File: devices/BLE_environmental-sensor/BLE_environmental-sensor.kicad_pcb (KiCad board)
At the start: 2 copper layers, 55 x 28 mm, 14 parts, among them Q1 Q_PMOS_GSD, U1 BGM220SC12WGA2R, U2 SHT4x, U3 STCC4, U4 LPS22DF, Y1 32.768kHz

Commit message: Finsihes version A.0 of the BLE sensor
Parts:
- removed Q1: Q_PMOS_GSD, Package_TO_SOT_SMD:TSOT-23
- removed Y1: 32.768kHz, Crystal:Crystal_SMD_3215-2Pin_3.2x1.5mm
- added C6: 100u, Capacitor_SMD:C_1206_3216Metric, F.Cu at (119.5, 94.0)
- added C7: 100n, Capacitor_SMD:C_0603_1608Metric, F.Cu at (123.8, 89.9)
- added J1: Samtec FTSM, Connector:Tag-Connect_TC2050-IDC-NL_2x05_P1.27mm_Vertical, F.Cu at (113.0, 79.2)
- added R2: 10k, Resistor_SMD:R_0603_1608Metric, F.Cu at (105.5, 75.3)
- added R3: 1M, Resistor_SMD:R_0603_1608Metric, F.Cu at (130.9, 93.2)
- added R4: 10k, Resistor_SMD:R_0603_1608Metric, F.Cu at (116.4, 89.8)
- added REF**: OSHW-Logo_19x20mm_SilkScreen, Symbol:OSHW-Logo_19x20mm_SilkScreen, B.Cu at (143.0, 84.0)
- added TP1: RCUCTE, custom:RCUCTE, F.Cu at (107.7, 95.9)
- added TP2: RCUCTE, custom:RCUCTE, F.Cu at (102.4, 94.1)
- added TP3: RCUCTE, custom:RCUCTE, F.Cu at (107.7, 93.9)
- added TP4: RCUCTE, custom:RCUCTE, F.Cu at (105.7, 72.7)
- added TP5: RCUCTE, custom:RCUCTE, F.Cu at (108.5, 72.7)
- added TP6: RCUCTE, custom:RCUCTE, F.Cu at (109.2, 83.8)
- added U5: TPS61291DVR, Package_SON:WSON-6-1EP_2x2mm_P0.65mm_EP1x1.6mm_ThermalVias, F.Cu at (115.0, 93.1)
- added U6: MX25R8035FM1IL0, Package_SO:JEITA_SOIC-8_3.9x4.9mm_P1.27mm, F.Cu at (128.3, 88.8)
- added kibuzzard-6A3D4B32: G***, kibuzzard-6A3D4B32, F.Cu at (110.8, 72.7)
- added kibuzzard-6A3D4B40: G***, kibuzzard-6A3D4B40, F.Cu at (103.3, 72.7)
- added kibuzzard-6A3D4B4B: G***, kibuzzard-6A3D4B4B, F.Cu at (102.4, 92.4)
- added kibuzzard-6A3D4B61: G***, kibuzzard-6A3D4B61, F.Cu at (105.4, 93.9)
- added kibuzzard-6A3D4B8C: G***, kibuzzard-6A3D4B8C, F.Cu at (105.3, 95.9)
- added kibuzzard-6A3D4E4D: G***, kibuzzard-6A3D4E4D, B.Cu at (113.0, 84.0)
- BT1: footprint custom:BatteryHolder_MPD_BK-912 -> custom:BatteryHolder_TE_BAT-HLD-001
- R1: value 0 -> 10k; footprint Resistor_SMD:R_01005_0402Metric -> Resistor_SMD:R_0603_1608Metric
- U1: value BGM220SC12WGA2R -> BGM220PC22HNA2; footprint custom:SiliconLab_BGM220SC12WGA2R -> custom:SiliconLab_BGM220P
- moved C1 61.0 mm to (117.3, 94.0), turned to 90 degrees
- moved C2 56.4 mm to (112.7, 94.0), turned to 90 degrees
- moved C3 51.0 mm to (104.6, 89.7)
- moved C4 50.4 mm to (104.6, 80.9), turned to 0 degrees
- moved L1 50.1 mm to (110.4, 94.7), turned to 90 degrees
- moved U2 48.4 mm to (104.6, 77.3), turned to -90 degrees
- moved U3 47.5 mm to (104.6, 86.7), turned to 180 degrees
- moved C5 46.7 mm to (104.6, 79.3)
- moved U4 46.5 mm to (104.6, 82.9)
- moved R1 30.8 mm to (108.5, 75.3), turned to 180 degrees
- moved BT1 23.3 mm to (145.2, 83.0), turned to -90 degrees
- moved U1 12.7 mm to (125.0, 77.5)
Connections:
- BT1 pad 1: VBAT -> VDD
- L1 pad 2: Net-(U5-SW) -> /SW
- R1 pad 1: Net-(U1-RF_2G4) -> VDD
- R1 pad 2: Net-(U1-ANT_IN) -> /SCL
- U1 pad 1: unconnected-(U1-NC-Pad1) -> GND
- U1 pad 12: unconnected-(U1-PA01-Pad12) -> GND
- U1 pad 13: unconnected-(U1-PA02-Pad13) -> VDD
- U1 pad 14: unconnected-(U1-DECOUPLE-Pad14) -> /UART_TX
- U1 pad 15: unconnected-(U1-PA03-Pad15) -> /UART_RX
- U1 pad 2: Net-(U1-ANT_IN) -> /SDA
- U1 pad 20: unconnected-(U1-PA08-Pad20) -> GND
- U1 pad 22: VDD -> /MOSI
- U1 pad 23: VDD -> /SPI_CLK
- U1 pad 24: unconnected-(U1-PD03-Pad24) -> /MISO
- U1 pad 25: unconnected-(U1-PD02-Pad25) -> /~{CS}
- U1 pad 26: /XTAL1 -> /PTI_DATA
- U1 pad 27: /XTAL0 -> /PTI_FRAME
- U1 pad 3: Net-(U1-RF_2G4) -> /SCL
- U1 pad 31: unconnected-(U1-PC03-Pad31) -> GND
- U1 pad 4: GND -> /3V3_EN
- U1 pad 5: GND -> /DT_READY
- U3 pad 1: unconnected-(U3-SCL-Pad1) -> /SCL
- U3 pad 5: unconnected-(U3-SDA-Pad5) -> /SDA
- U4 pad 2: unconnected-(U4-SCL-Pad2) -> /SCL
- U4 pad 4: unconnected-(U4-SDA-Pad4) -> /SDA
- U4 pad 5: unconnected-(U4-SA0-Pad5) -> GND
- U4 pad 7: unconnected-(U4-INT_DRDY-Pad7) -> /DT_READY
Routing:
- net VDD: track 0.00 -> 77.6 mm
- net /SCL: track 0.00 -> 36.3 mm, vias 0 -> 4
- net /3V3_EN: track 0.00 -> 34.7 mm
- net /SDA: track 0.00 -> 34.6 mm, vias 0 -> 2
- net /DT_READY: track 0.00 -> 24.9 mm, vias 0 -> 2
- net /~{CS}: track 0.00 -> 20.7 mm
- net /PTI_DATA: track 0.00 -> 20.3 mm, vias 0 -> 2
- net /PTI_FRAME: track 0.00 -> 18.0 mm, vias 0 -> 2
- net /SPI_CLK: track 0.00 -> 16.8 mm
- net /MISO: track 0.00 -> 15.2 mm
- net /UART_RX: track 0.00 -> 15.1 mm, vias 0 -> 2
- net GND: track 0.00 -> 14.0 mm, vias 71 -> 171
- net /UART_TX: track 0.00 -> 13.1 mm, vias 0 -> 2
- net /MOSI: track 0.00 -> 12.9 mm
- net +3.3V: track 0.00 -> 8.90 mm
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- added copper zone on F.Cu, net +3.3V
- added copper zone on F.Cu, net /SW
- added copper zone on F.Cu, net VDD
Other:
- board size 55 x 28 mm -> 54.5 x 28 mm

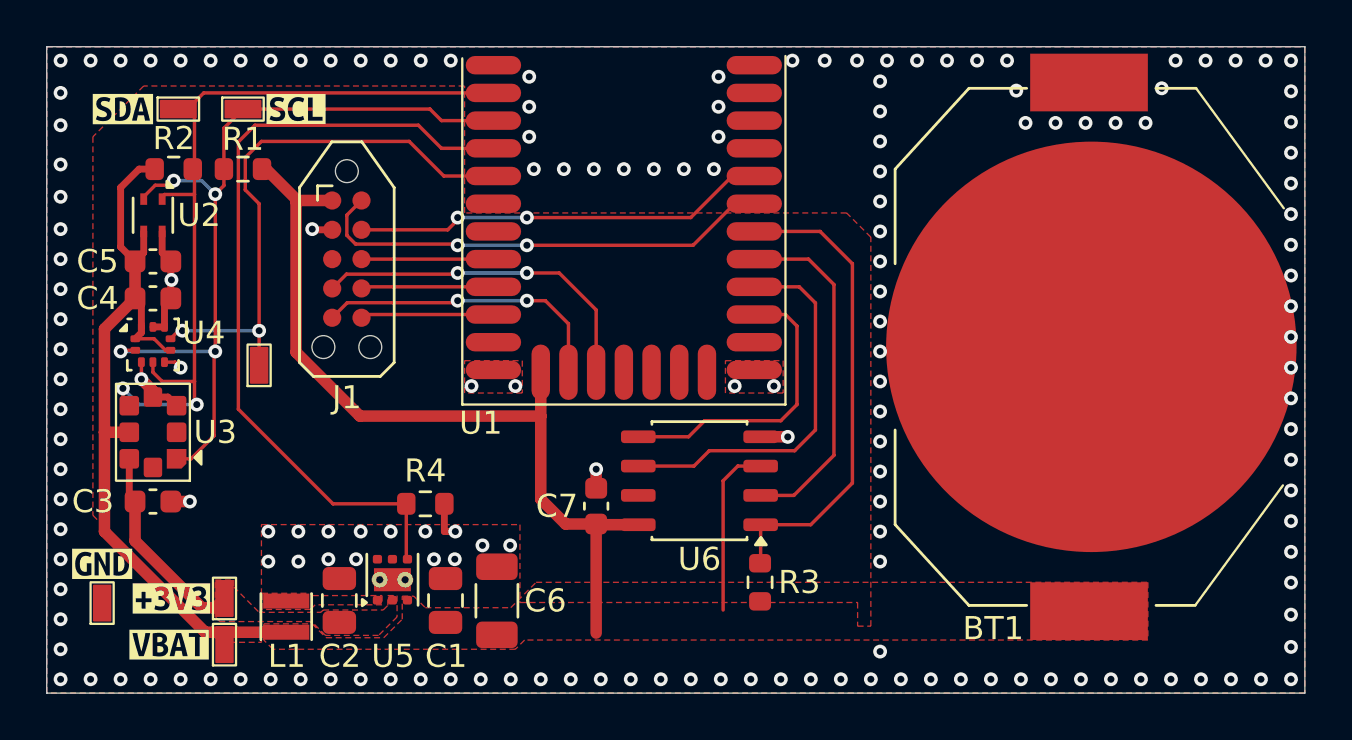
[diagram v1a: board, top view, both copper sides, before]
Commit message: Changes the boost converter for the device for better low power performance.
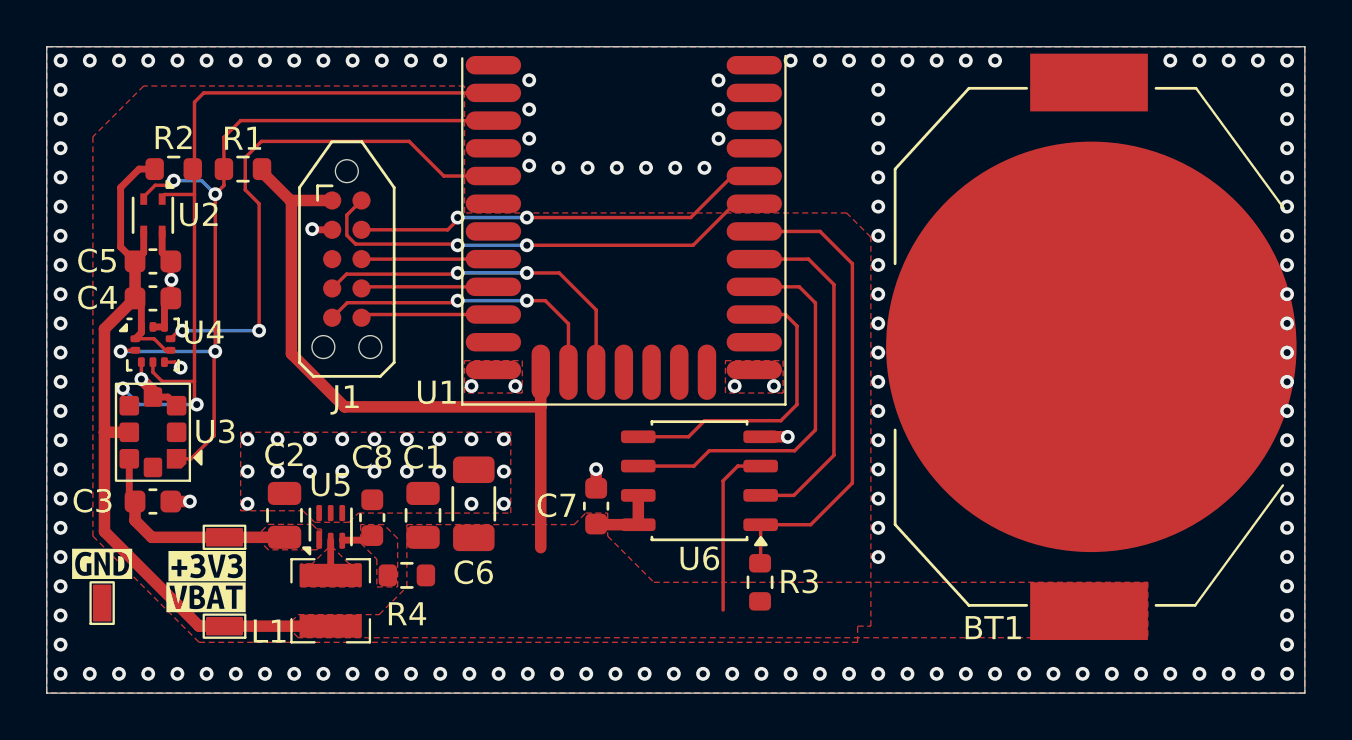
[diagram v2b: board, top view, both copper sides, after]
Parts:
- removed the REF** at (143.0, 84.0)
- removed TP4, TP5, TP6: RCUCTE, custom:RCUCTE
- removed kibuzzard-6A3D4B32: G***, kibuzzard-6A3D4B32
- removed kibuzzard-6A3D4B40: G***, kibuzzard-6A3D4B40
- added C8: 100n, Capacitor_SMD:C_0603_1608Metric, F.Cu at (114.1, 90.4)
- added REF**: OSHW-Logo_11.4x12mm_SilkScreen, Symbol:OSHW-Logo_11.4x12mm_SilkScreen, B.Cu at (133.0, 84.5)
- added kibuzzard-6A7308BE: G***, kibuzzard-6A7308BE, B.Cu at (148.6, 83.9)
- C2: value 22u -> 10u
- L1: value 3u3 -> 4u7; footprint Inductor_SMD:L_Taiyo-Yuden_MD-2020 -> custom:L_Bourns-SRN3015
- R4: value 10k -> 390
- U5: value TPS61291DVR -> TPS610981DSE; footprint Package_SON:WSON-6-1EP_2x2mm_P0.65mm_EP1x1.6mm_ThermalVias -> Package_SON:WSON-6_1.5x1.5mm_P0.5mm
- moved C2 4.39 mm to (110.3, 90.3)
- moved C6 4.32 mm to (118.5, 89.8)
- moved C1 3.81 mm to (116.3, 90.3)
- moved U5 3.52 mm to (112.3, 90.8)
- moved R4 3.20 mm to (115.6, 92.9), turned to 180 degrees
- moved TP3 2.65 mm to (107.7, 91.2), turned to 180 degrees
- moved kibuzzard-6A3D4B8C 2.60 mm to (106.9, 93.8)
- moved kibuzzard-6A3D4B61 2.09 mm to (107.0, 92.5)
- moved L1 2.04 mm to (112.3, 94.0)
- moved TP1 0.80 mm to (107.7, 95.1), turned to 180 degrees
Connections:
- R4 pad 1: /3V3_EN -> VDD
- R4 pad 2: GND -> /VIN
- U1 pad 4: /3V3_EN -> unconnected-(U1-PB02-Pad4)
- U5 pad 1: /SW -> +3.3V
- U5 pad 2: +3.3V -> /SW
- U5 pad 3: VDD -> /VIN
- U5 pad 4: /3V3_EN -> GND
- U5 pad 5: GND -> unconnected-(U5-VSUB-Pad5)
- U6 pad 7: unconnected-(U6-~{RESET}/SIO3-Pad7) -> VDD
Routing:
- net /3V3_EN: track 34.7 -> 0.00 mm
- net VDD: track 77.6 -> 75.5 mm
- net GND: track 14.0 -> 12.3 mm
- net /SW: track 0.00 -> 1.53 mm
- net /DT_READY: track 24.9 -> 23.4 mm
- net /VIN: track 0.00 -> 1.34 mm
- net +3.3V: track 8.90 -> 9.55 mm
- net /SCL: track 36.3 -> 35.7 mm
- added copper zone on F.Cu, net /VIN
